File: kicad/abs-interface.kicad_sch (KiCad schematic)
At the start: 25 parts

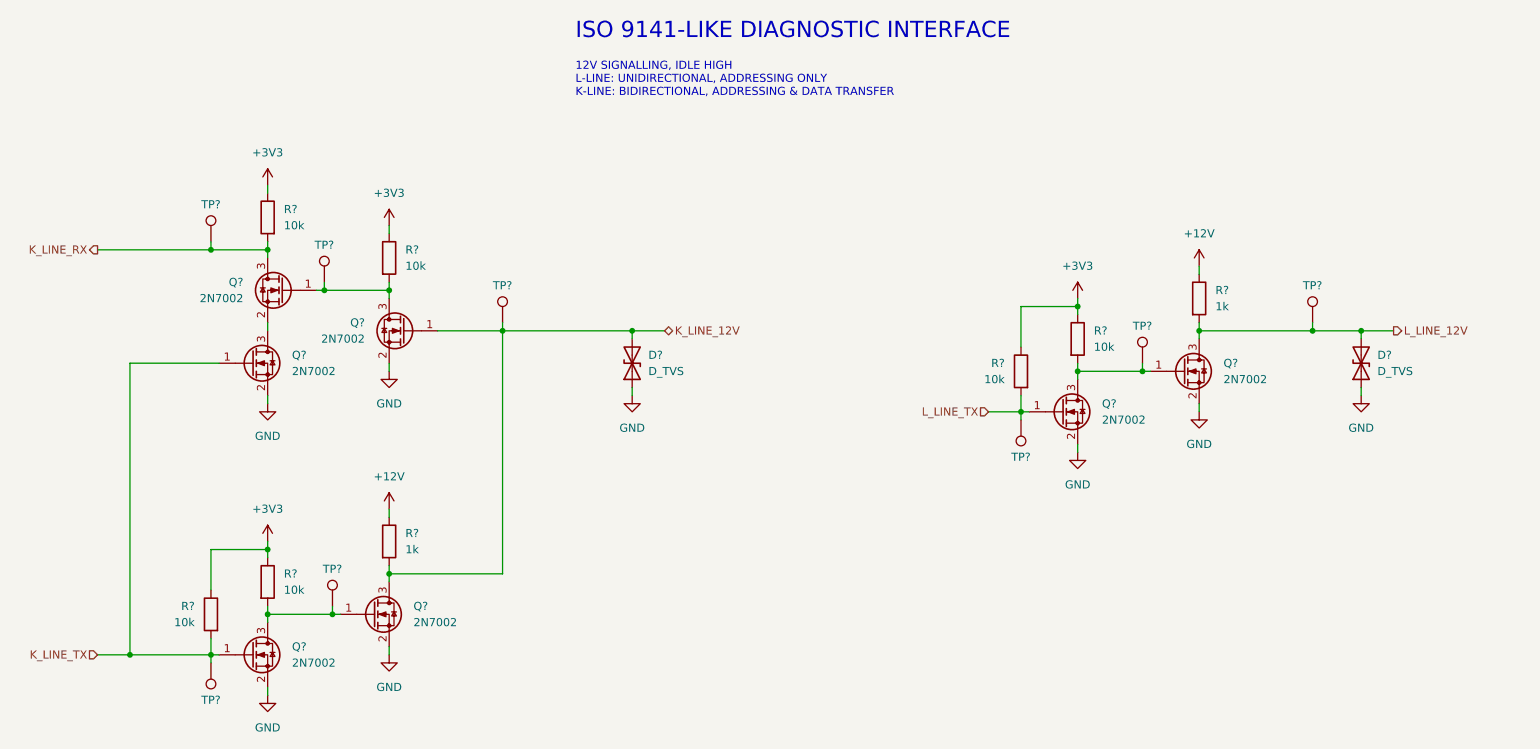
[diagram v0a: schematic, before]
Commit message: Update ABS diagnostic interface
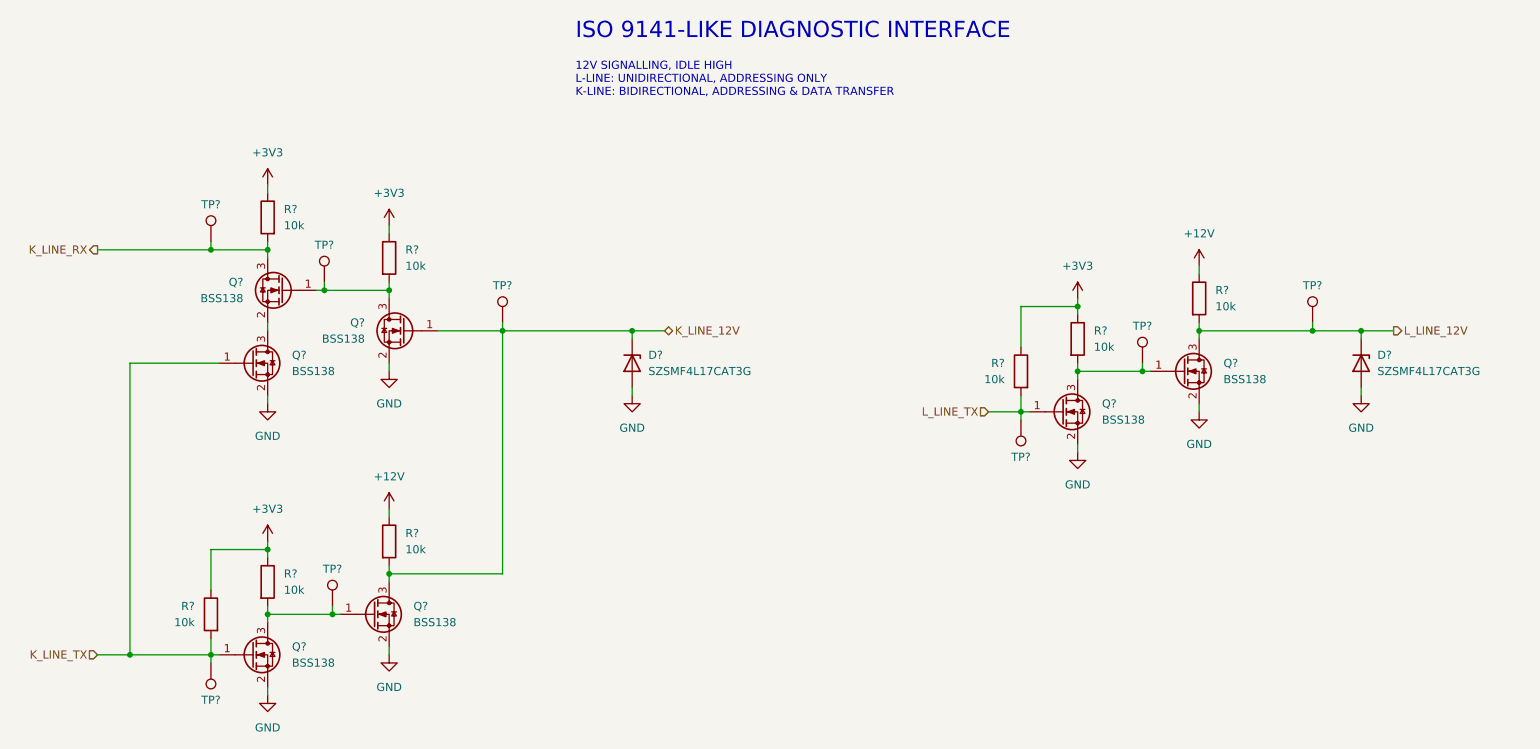
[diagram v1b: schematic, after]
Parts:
- removed D? (x2): D_TVS, symbol bmw-e36-abs-module:D_TVS
- removed Q? (x7): 2N7002, Package_TO_SOT_SMD:SOT-23, symbol symbols:2N7002
- added D? (x2): SZSMF4L17CAT3G, Diode_SMD:D_SOD-123F, symbol symbols:D_Zener
- added Q? (x7): BSS138, Package_TO_SOT_SMD:SOT-323_SC-70, symbol symbols:BSS138
- R? (x2): value 1k -> 10k
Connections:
- net GND: now also D?.2 (A), D?.2 (A), Q?.2 (S), Q?.2 (S), Q?.2 (S), Q?.2 (S), Q?.2 (S), Q?.2 (S)
- net K_LINE_12V: now also D?.1 (K), Q?.1 (G), Q?.3 (D)
- net K_LINE_RX: now also Q?.3 (D)
- net K_LINE_TX: now also Q?.1 (G), Q?.1 (G)
- net L_LINE_12V: now also D?.1 (K), Q?.3 (D)
- net L_LINE_TX: now also Q?.1 (G)
- net at R?.2, TP?.1: now also Q?.1 (G), Q?.3 (D) (x3)
- new net: Q?.2 (S), Q?.3 (D)

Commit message: Update connector; annotate and assign footprints
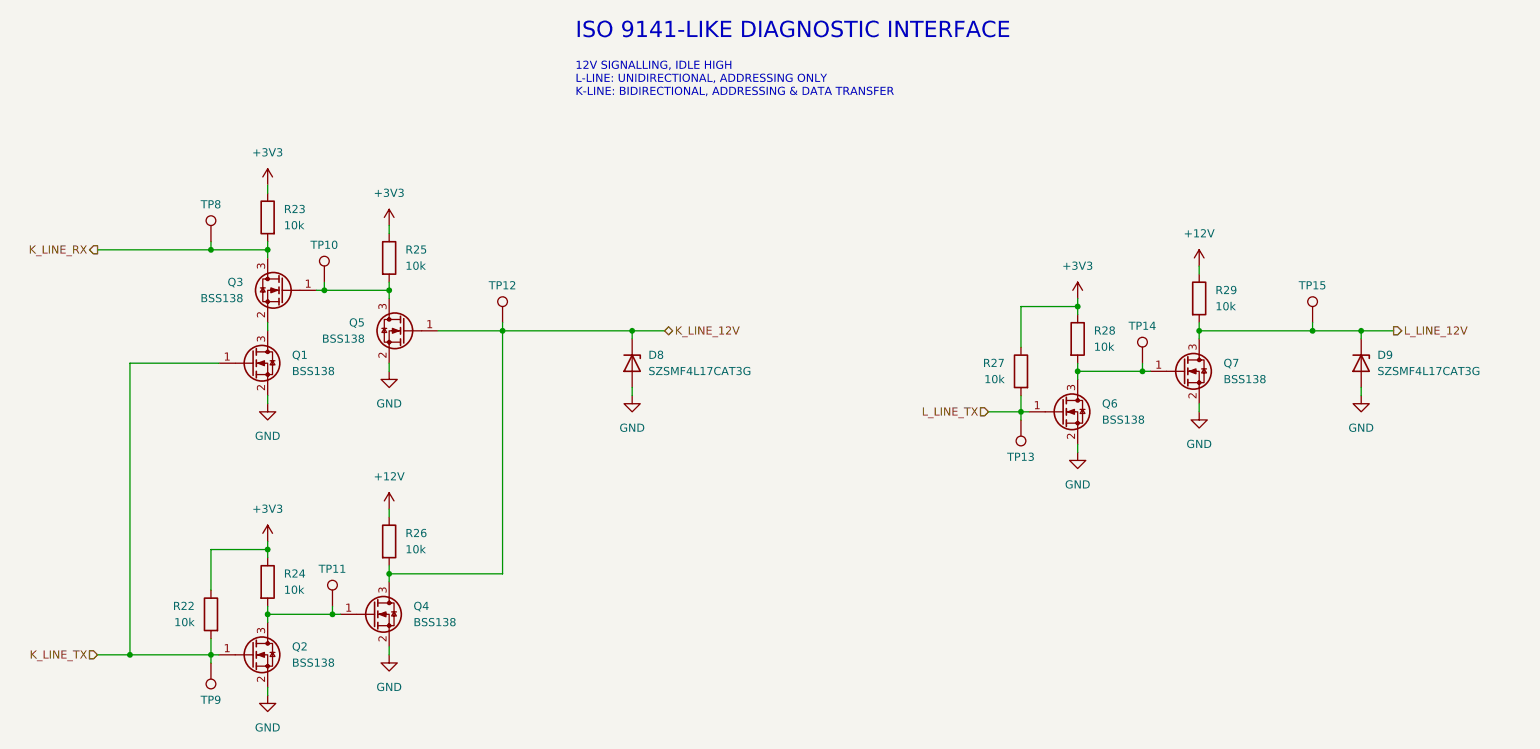
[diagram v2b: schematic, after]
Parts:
- R22, R23, R24, R25, R26, R27, R28, R29: renamed from R?; footprint (none) -> Resistor_SMD:R_0603_1608Metric
- TP10, TP11, TP12, TP13, TP14, TP15, TP8, TP9: renamed from TP?; footprint (none) -> TestPoint:TestPoint_Pad_D2.0mm
- gave numbers to parts that had none: 9

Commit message: Add optional RC filter to pressure sensor inputs
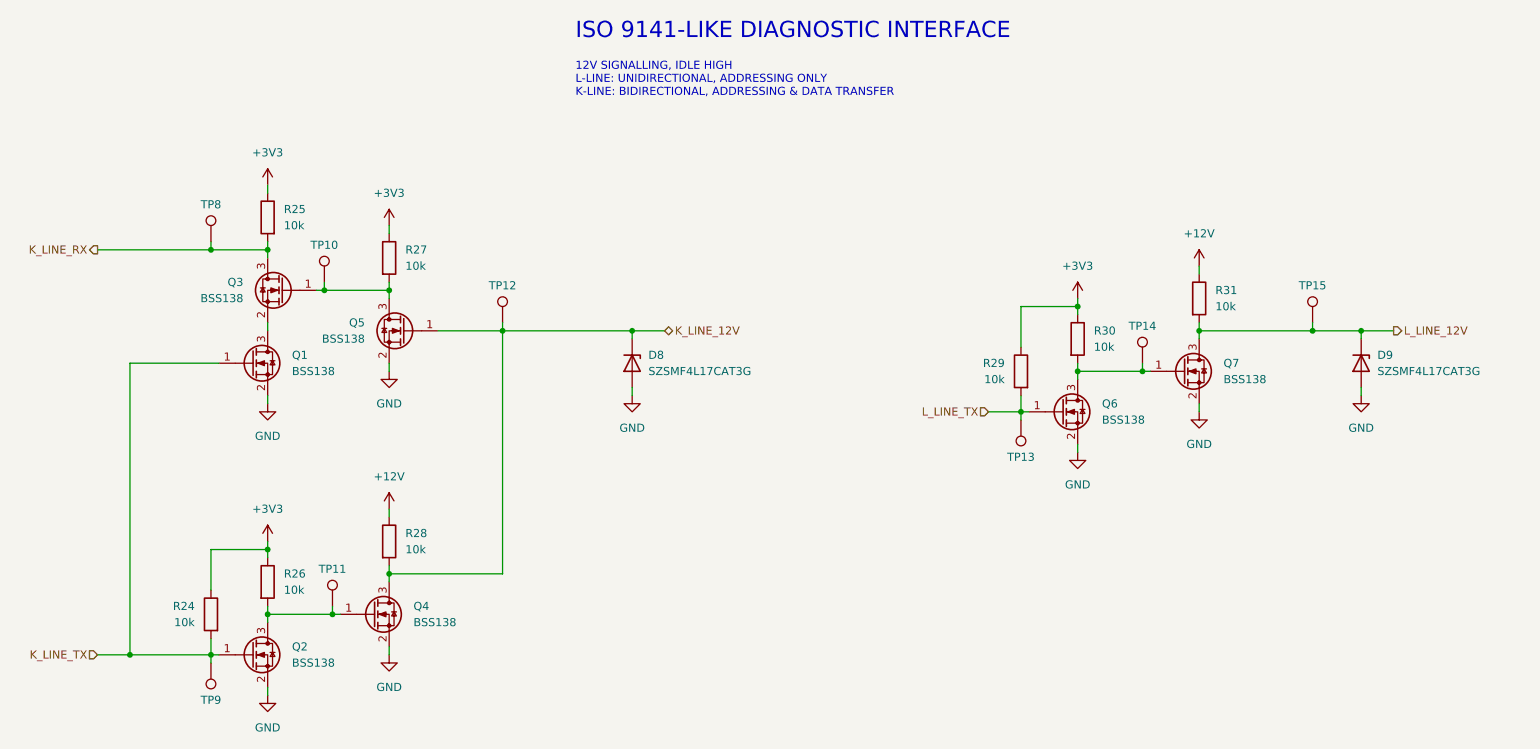
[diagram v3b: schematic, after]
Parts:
- renumbered R22 to R24, R23 to R25, R24 to R26, R25 to R27, R26 to R28, R27 to R29, R28 to R30, R29 to R31
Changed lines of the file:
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@@
 		(dnp no)
 		(fields_autoplaced yes)
-		(property "Reference" "#PWR048"
+		(property "Reference" "#PWR050"
 			(at 287.02 107.95 0)
 			(hide yes)
@@
 			(project "bmw-e36-abs-adapter"
 				(path "/325be93f-b4a6-4f2b-83c3-2ccd33e5cc03/764d85a6-8b64-4d79-a3de-d53eaa3c0d1e"
-					(reference "#PWR048")
+					(reference "#PWR050")
 					(unit 1)
 				)
@@
 		(dnp no)
 		(fields_autoplaced yes)
-		(property "Reference" "#PWR038"
+		(property "Reference" "#PWR040"
 			(at 140.97 132.08 0)
 			(hide yes)
@@
 			(project "bmw-e36-abs-adapter"
 				(path "/325be93f-b4a6-4f2b-83c3-2ccd33e5cc03/764d85a6-8b64-4d79-a3de-d53eaa3c0d1e"
-					(reference "#PWR038")
+					(reference "#PWR040")
 					(unit 1)
 				)
@@
 		(dnp no)
 		(fields_autoplaced yes)
-		(property "Reference" "#PWR040"
+		(property "Reference" "#PWR042"
 			(at 140.97 177.8 0)
 			(hide yes)
@@
 			(project "bmw-e36-abs-adapter"
 				(path "/325be93f-b4a6-4f2b-83c3-2ccd33e5cc03/764d85a6-8b64-4d79-a3de-d53eaa3c0d1e"
-					(reference "#PWR040")
+					(reference "#PWR042")
 					(unit 1)
 				)
@@
 		(in_pos_files yes)
 		(dnp no)
-		(property "Reference" "R27"
+		(property "Reference" "R29"
 			(at 256.54 119.3799 0)
 			(show_name no)
@@
 			(project "bmw-e36-abs-adapter"
 				(path "/325be93f-b4a6-4f2b-83c3-2ccd33e5cc03/764d85a6-8b64-4d79-a3de-d53eaa3c0d1e"
-					(reference "R27")
+					(reference "R29")
 					(unit 1)
 				)
@@
 		(dnp no)
 		(fields_autoplaced yes)
-		(property "Reference" "#PWR043"
+		(property "Reference" "#PWR045"
 			(at 160.02 146.05 0)
 			(hide yes)
@@
 			(project "bmw-e36-abs-adapter"
 				(path "/325be93f-b4a6-4f2b-83c3-2ccd33e5cc03/764d85a6-8b64-4d79-a3de-d53eaa3c0d1e"
-					(reference "#PWR043")
+					(reference "#PWR045")
 					(unit 1)
 				)
@@
 		(dnp no)
 		(fields_autoplaced yes)
-		(property "Reference" "#PWR037"
+		(property "Reference" "#PWR039"
 			(at 140.97 95.25 0)
 			(hide yes)
@@
 			(project "bmw-e36-abs-adapter"
 				(path "/325be93f-b4a6-4f2b-83c3-2ccd33e5cc03/764d85a6-8b64-4d79-a3de-d53eaa3c0d1e"
-					(reference "#PWR037")
+					(reference "#PWR039")
 					(unit 1)
 				)
@@
 		(dnp no)
 		(fields_autoplaced yes)
-		(property "Reference" "#PWR047"
+		(property "Reference" "#PWR049"
 			(at 267.97 139.7 0)
 			(hide yes)
@@
 			(project "bmw-e36-abs-adapter"
 				(path "/325be93f-b4a6-4f2b-83c3-2ccd33e5cc03/764d85a6-8b64-4d79-a3de-d53eaa3c0d1e"
-					(reference "#PWR047")
+					(reference "#PWR049")
 					(unit 1)
 				)
@@
 		(dnp no)
 		(fields_autoplaced yes)
-		(property "Reference" "R24"
+		(property "Reference" "R26"
 			(at 143.51 152.3999 0)
 			(show_name no)
@@
 			(project "bmw-e36-abs-adapter"
 				(path "/325be93f-b4a6-4f2b-83c3-2ccd33e5cc03/764d85a6-8b64-4d79-a3de-d53eaa3c0d1e"
-					(reference "R24")
+					(reference "R26")
 					(unit 1)
 				)
@@
 		(dnp no)
 		(fields_autoplaced yes)
-		(property "Reference" "R29"
+		(property "Reference" "R31"
 			(at 289.56 107.9499 0)
 			(show_name no)
@@
 			(project "bmw-e36-abs-adapter"
 				(path "/325be93f-b4a6-4f2b-83c3-2ccd33e5cc03/764d85a6-8b64-4d79-a3de-d53eaa3c0d1e"
-					(reference "R29")
+					(reference "R31")
 					(unit 1)
 				)
@@
 		(dnp no)
 		(fields_autoplaced yes)
-		(property "Reference" "#PWR042"
+		(property "Reference" "#PWR044"
 			(at 160.02 127 0)
 			(hide yes)
@@
 			(project "bmw-e36-abs-adapter"
 				(path "/325be93f-b4a6-4f2b-83c3-2ccd33e5cc03/764d85a6-8b64-4d79-a3de-d53eaa3c0d1e"
-					(reference "#PWR042")
+					(reference "#PWR044")
 					(unit 1)
 				)
@@
 		(dnp no)
 		(fields_autoplaced yes)
-		(property "Reference" "#PWR045"
+		(property "Reference" "#PWR047"
 			(at 198.12 130.81 0)
 			(hide yes)
@@
 			(project "bmw-e36-abs-adapter"
 				(path "/325be93f-b4a6-4f2b-83c3-2ccd33e5cc03/764d85a6-8b64-4d79-a3de-d53eaa3c0d1e"
-					(reference "#PWR045")
+					(reference "#PWR047")
 					(unit 1)
 				)
@@
 		(in_pos_files yes)
 		(dnp no)
-		(property "Reference" "R25"
+		(property "Reference" "R27"
 			(at 162.56 101.5999 0)
 			(show_name no)
@@
 			(project "bmw-e36-abs-adapter"
 				(path "/325be93f-b4a6-4f2b-83c3-2ccd33e5cc03/764d85a6-8b64-4d79-a3de-d53eaa3c0d1e"
-					(reference "R25")
+					(reference "R27")
 					(unit 1)
 				)
@@
 		(dnp no)
 		(fields_autoplaced yes)
-		(property "Reference" "#PWR046"
+		(property "Reference" "#PWR048"
 			(at 267.97 113.03 0)
 			(hide yes)
@@
 			(project "bmw-e36-abs-adapter"
 				(path "/325be93f-b4a6-4f2b-83c3-2ccd33e5cc03/764d85a6-8b64-4d79-a3de-d53eaa3c0d1e"
-					(reference "#PWR046")
+					(reference "#PWR048")
 					(unit 1)
 				)
@@
 		(dnp no)
 		(fields_autoplaced yes)
-		(property "Reference" "R28"
+		(property "Reference" "R30"
 			(at 270.51 114.2999 0)
 			(show_name no)
@@
 			(project "bmw-e36-abs-adapter"
 				(path "/325be93f-b4a6-4f2b-83c3-2ccd33e5cc03/764d85a6-8b64-4d79-a3de-d53eaa3c0d1e"
-					(reference "R28")
+					(reference "R30")
 					(unit 1)
 				)
@@
 		(dnp no)
 		(fields_autoplaced yes)
-		(property "Reference" "#PWR044"
+		(property "Reference" "#PWR046"
 			(at 160.02 171.45 0)
 			(hide yes)
@@
 			(project "bmw-e36-abs-adapter"
 				(path "/325be93f-b4a6-4f2b-83c3-2ccd33e5cc03/764d85a6-8b64-4d79-a3de-d53eaa3c0d1e"
-					(reference "#PWR044")
+					(reference "#PWR046")
 					(unit 1)
 				)
@@
 		(dnp no)
 		(fields_autoplaced yes)
-		(property "Reference" "#PWR049"
+		(property "Reference" "#PWR051"
 			(at 287.02 133.35 0)
 			(hide yes)
@@
 			(project "bmw-e36-abs-adapter"
 				(path "/325be93f-b4a6-4f2b-83c3-2ccd33e5cc03/764d85a6-8b64-4d79-a3de-d53eaa3c0d1e"
-					(reference "#PWR049")
+					(reference "#PWR051")
 					(unit 1)
 				)
@@
 		(dnp no)
 		(fields_autoplaced yes)
-		(property "Reference" "#PWR039"
+		(property "Reference" "#PWR041"
 			(at 140.97 151.13 0)
 			(hide yes)
@@
 			(project "bmw-e36-abs-adapter"
 				(path "/325be93f-b4a6-4f2b-83c3-2ccd33e5cc03/764d85a6-8b64-4d79-a3de-d53eaa3c0d1e"
-					(reference "#PWR039")
+					(reference "#PWR041")
 					(unit 1)
 				)
@@
 		(dnp no)
 		(fields_autoplaced yes)
-		(property "Reference" "#PWR050"
+		(property "Reference" "#PWR052"
 			(at 312.42 130.81 0)
 			(hide yes)
@@
 			(project "bmw-e36-abs-adapter"
 				(path "/325be93f-b4a6-4f2b-83c3-2ccd33e5cc03/764d85a6-8b64-4d79-a3de-d53eaa3c0d1e"
-					(reference "#PWR050")
+					(reference "#PWR052")
 					(unit 1)
 				)
@@
 		(dnp no)
 		(fields_autoplaced yes)
-		(property "Reference" "#PWR041"
+		(property "Reference" "#PWR043"
 			(at 160.02 101.6 0)
 			(hide yes)
@@
 			(project "bmw-e36-abs-adapter"
 				(path "/325be93f-b4a6-4f2b-83c3-2ccd33e5cc03/764d85a6-8b64-4d79-a3de-d53eaa3c0d1e"
-					(reference "#PWR041")
+					(reference "#PWR043")
 					(unit 1)
 				)
@@
 		(dnp no)
 		(fields_autoplaced yes)
-		(property "Reference" "R26"
+		(property "Reference" "R28"
 			(at 162.56 146.0499 0)
 			(show_name no)
@@
 			(project "bmw-e36-abs-adapter"
 				(path "/325be93f-b4a6-4f2b-83c3-2ccd33e5cc03/764d85a6-8b64-4d79-a3de-d53eaa3c0d1e"
-					(reference "R26")
+					(reference "R28")
 					(unit 1)
 				)
@@
 		(in_pos_files yes)
 		(dnp no)
-		(property "Reference" "R23"
+		(property "Reference" "R25"
 			(at 143.51 95.2499 0)
 			(show_name no)
@@
 			(project "bmw-e36-abs-adapter"
 				(path "/325be93f-b4a6-4f2b-83c3-2ccd33e5cc03/764d85a6-8b64-4d79-a3de-d53eaa3c0d1e"
-					(reference "R23")
+					(reference "R25")
 					(unit 1)
 				)
@@
 		(in_pos_files yes)
 		(dnp no)
-		(property "Reference" "R22"
+		(property "Reference" "R24"
 			(at 129.54 157.4799 0)
 			(show_name no)
@@
 			(project "bmw-e36-abs-adapter"
 				(path "/325be93f-b4a6-4f2b-83c3-2ccd33e5cc03/764d85a6-8b64-4d79-a3de-d53eaa3c0d1e"
-					(reference "R22")
-					(unit 1)
-				)
+					(reference "R24")
+					(unit 1)
+				)

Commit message: Update part numbers and fix ERC issues
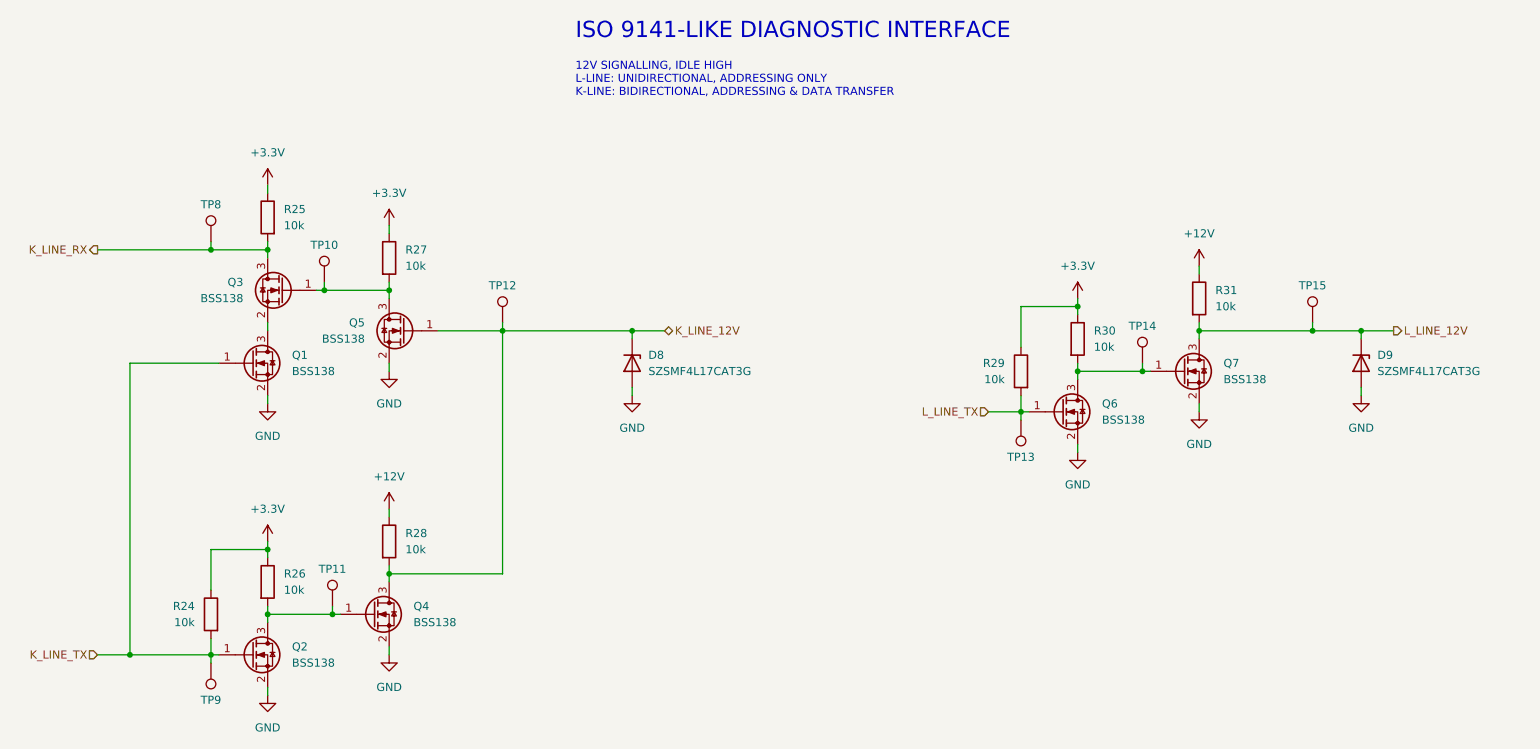
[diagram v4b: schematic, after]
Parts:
- R24, R25, R26, R27, R28, R29, R30, R31: Manufacturer (none) -> Panasonic; Part Number (none) -> ERJ-3EKF1002V
- TP10, TP11, TP12, TP13, TP14, TP15, TP8, TP9: now left out of the parts list
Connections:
- net +3V3 renamed +3.3V
